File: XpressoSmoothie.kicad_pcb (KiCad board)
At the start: 2 copper layers, 99.7 x 99.7 mm, 130 parts, among them J1 HEADER_4, J10 HEADER_3X2, J11 Pwr_in, J12 HEADER_4, J13 HEADER_4X2, J14 HEADER_3X2, J15 HEADER_4, J16 HEADER_4, J17 HEADER_4, J172 HEADER_2, J18 HEADER_4, J19 HEADER_2, J2 HEADER_4, J20 HEADER_2, J21 HEADER_2, J22 HEADER_2, J23 HEADER_4, J232 HEADER_2, J24 HEADER_4, J25 HEADER_4, J252 HEADER_2, J26 USB, J27 HEADER_4, J28 MICROSD-MOLEX, J3 HEADER_3, J4 HEADER_3X2, J5 HEADER_3X2, J6 LPCXPRESSO_GENERIC_HEADER, J7 HEADER_4, J8 HEADER_4, J9 HEADER_3X2, M1 LOGO_OSHW, M2 LOGO_OSHW, Q1 IRLB 8743, Q2 IRLB 8743, Q3 IRLB 8743, Q4 IRLB 8743, SW1 SW_PUSH, SW2 SW_PUSH, U1 POLOLU_A4988, U10 TC4422A, U11 TC4422A, U12 LM1117-3.3, U2 POLOLU_A4988, U3 POLOLU_A4988, U4 POLOLU_A4988, U5 POLOLU_A4988, U7 LM7809CT, U8 TC4422A, U9 TC4422A

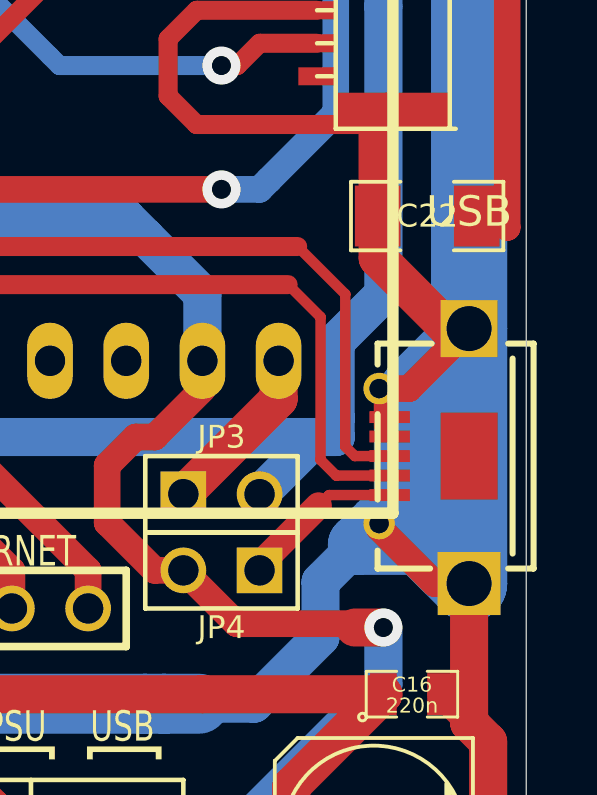
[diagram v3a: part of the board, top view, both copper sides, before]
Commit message: Moved USB so that PCB edge line lines up with the edge of the PCB. Also removed silkscreen lines that hung over the edge. Closes #15.
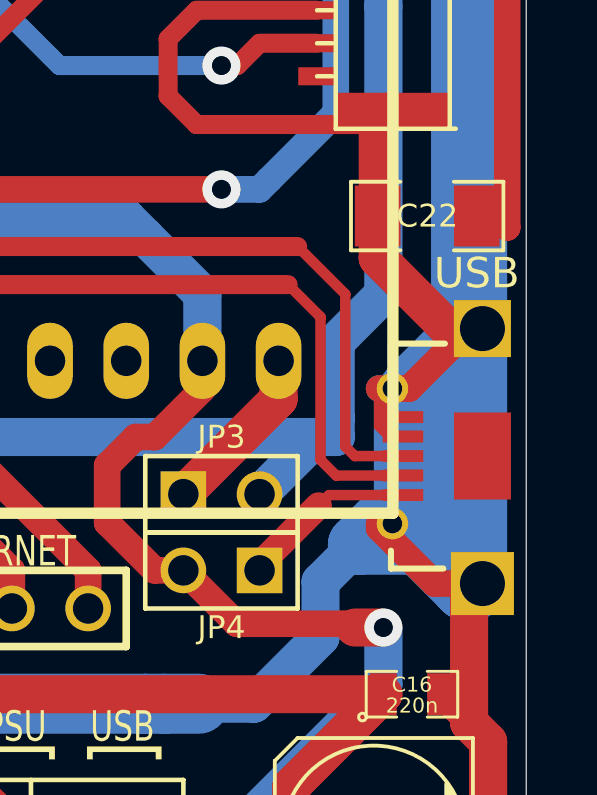
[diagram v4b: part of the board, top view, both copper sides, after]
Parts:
- J26: footprint USB_MICRO_RMC -> USB_MICRO_RMC_noedge
- moved J26 0.44 mm to (170.0, 120.0)
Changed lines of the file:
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@@
     (links 344)
     (no_connects 11)
-    (area 56.388 52.51262 179.864657 163.2712)
+    (area 71.742299 53.962299 171.462701 153.682701)
     (thickness 1.6)
     (drawings 31)
@@
   )
   (setup
-    (last_trace_width 2.54)
+    (last_trace_width 0.635)
     (user_trace_width 0.35)
     (user_trace_width 0.889)
@@
     (add_net ZMIN)
   )
-  (module USB_MICRO_RMC (layer F.Cu)
-    (at 169.545 120.015 180)
-    (fp_text reference J26 (at 0 -7.44982 180) (layer F.SilkS) hide
-      (effects (font (size 1.016 1.016) (thickness 0.127)))
-    )
-    (fp_text value USB (at 0 8.15086 180) (layer F.SilkS)
-      (effects (font (size 1.016 1.016) (thickness 0.127)))
-    )
-    (fp_line (start -1.45034 -3.2512) (end -1.45034 3.2512) (layer F.SilkS) (width 0.2032))
-    (fp_line (start 1.24968 3.74904) (end 3.05054 3.74904) (layer F.SilkS) (width 0.2032))
-    (fp_line (start 3.05054 3.74904) (end 3.05054 3.05054) (layer F.SilkS) (width 0.2032))
-    (fp_line (start 3.05054 -1.45034) (end 3.05054 1.39954) (layer F.SilkS) (width 0.2032))
-    (fp_line (start 1.30048 -3.74904) (end 3.05054 -3.74904) (layer F.SilkS) (width 0.2032))
-    (fp_line (start 3.05054 -3.74904) (end 3.05054 -3.1496) (layer F.SilkS) (width 0.2032))
-    (fp_line (start -2.14884 3.74904) (end -1.30048 3.74904) (layer F.SilkS) (width 0.2032))
-    (fp_line (start -2.14884 3.74904) (end -2.14884 -3.74904) (layer F.SilkS) (width 0.2032))
-    (fp_line (start -2.14884 -3.74904) (end -1.30048 -3.74904) (layer F.SilkS) (width 0.2032))
-    (pad 5 smd rect (at 0 0 180) (size 1.89992 2.90068)
-      (layers F.Cu F.Paste F.Mask)
-      (net 19 GND)
-    )
-    (pad 5 thru_hole rect (at 0 -4.24942 180) (size 2.10058 2.10058) (drill 1.50114)
-      (layers *.Cu *.Mask F.SilkS)
-      (net 19 GND)
-    )
-    (pad 5 thru_hole rect (at 0 4.24942 180) (size 1.89992 1.89992) (drill 1.50114)
-      (layers *.Cu *.Mask F.SilkS)
-      (net 19 GND)
-    )
-    (pad 5 thru_hole circle (at 2.99974 2.25044 180) (size 1.04902 1.04902) (drill 0.65024)
-      (layers *.Cu *.Mask F.SilkS)
-      (net 19 GND)
-    )
-    (pad 5 thru_hole circle (at 2.99974 -2.25044 180) (size 1.04902 1.04902) (drill 0.65024)
-      (layers *.Cu *.Mask F.SilkS)
-      (net 19 GND)
-    )
-    (pad 3 smd rect (at 2.64922 0 180) (size 1.34874 0.39878)
-      (layers F.Cu F.Paste F.Mask)
-      (net 119 USB-D+)
-    )
-    (pad 6 smd rect (at 2.64922 0.65024 180) (size 1.34874 0.39878)
-      (layers F.Cu F.Paste F.Mask)
-      (net 19 GND)
-    )
-    (pad 4 smd rect (at 2.64922 1.30048 180) (size 1.34874 0.39878)
-      (layers F.Cu F.Paste F.Mask)
-      (net 19 GND)
-    )
-    (pad 2 smd rect (at 2.64922 -0.65024 180) (size 1.34874 0.39878)
-      (layers F.Cu F.Paste F.Mask)
-      (net 120 USB-D-)
-    )
-    (pad 1 smd rect (at 2.64922 -1.30048 180) (size 1.34874 0.39878)
-      (layers F.Cu F.Paste F.Mask)
-      (net 52 N-0000014)
-    )
-    (model ..\KiCAD_Libraries\packages3d\rmc\misc\USB3075-30-Ak.wrl
-      (at (xyz 0.165 -0.155 0))
-      (scale (xyz 1 1 1))
-      (rotate (xyz 0 180 0))
-    )
-  )
   (module TO220_VERT_C (layer F.Cu)
     (at 92.202 137.795 270)
@@
     )
   )
+  (module USB_MICRO_RMC_noedge (layer F.Cu)
+    (at 169.9895 120.015 180)
+    (fp_text reference J26 (at 0 -7.44982 180) (layer F.SilkS) hide
+      (effects (font (size 1.016 1.016) (thickness 0.127)))
+    )
+    (fp_text value USB (at 0.1905 6.096 180) (layer F.SilkS)
+      (effects (font (size 1.016 1.016) (thickness 0.127)))
+    )
+    (fp_line (start 1.24968 3.74904) (end 3.05054 3.74904) (layer F.SilkS) (width 0.2032))
+    (fp_line (start 3.05054 3.74904) (end 3.05054 3.05054) (layer F.SilkS) (width 0.2032))
+    (fp_line (start 3.05054 -1.45034) (end 3.05054 1.39954) (layer F.SilkS) (width 0.2032))
+    (fp_line (start 1.30048 -3.74904) (end 3.05054 -3.74904) (layer F.SilkS) (width 0.2032))
+    (fp_line (start 3.05054 -3.74904) (end 3.05054 -3.1496) (layer F.SilkS) (width 0.2032))
+    (pad 5 smd rect (at 0 0 180) (size 1.89992 2.90068)
+      (layers F.Cu F.Paste F.Mask)
+      (net 19 GND)
+    )
+    (pad 5 thru_hole rect (at 0 -4.24942 180) (size 2.10058 2.10058) (drill 1.50114)
+      (layers *.Cu *.Mask F.SilkS)
+      (net 19 GND)
+    )
+    (pad 5 thru_hole rect (at 0 4.24942 180) (size 1.89992 1.89992) (drill 1.50114)
+      (layers *.Cu *.Mask F.SilkS)
+      (net 19 GND)
+    )
+    (pad 5 thru_hole circle (at 2.99974 2.25044 180) (size 1.04902 1.04902) (drill 0.65024)
+      (layers *.Cu *.Mask F.SilkS)
+      (net 19 GND)
+    )
+    (pad 5 thru_hole circle (at 2.99974 -2.25044 180) (size 1.04902 1.04902) (drill 0.65024)
+      (layers *.Cu *.Mask F.SilkS)
+      (net 19 GND)
+    )
+    (pad 3 smd rect (at 2.64922 0 180) (size 1.34874 0.39878)
+      (layers F.Cu F.Paste F.Mask)
+      (net 119 USB-D+)
+    )
+    (pad 6 smd rect (at 2.64922 0.65024 180) (size 1.34874 0.39878)
+      (layers F.Cu F.Paste F.Mask)
+      (net 19 GND)
+    )
+    (pad 4 smd rect (at 2.64922 1.30048 180) (size 1.34874 0.39878)
+      (layers F.Cu F.Paste F.Mask)
+      (net 19 GND)
+    )
+    (pad 2 smd rect (at 2.64922 -0.65024 180) (size 1.34874 0.39878)
+      (layers F.Cu F.Paste F.Mask)
+      (net 120 USB-D-)
+    )
+    (pad 1 smd rect (at 2.64922 -1.30048 180) (size 1.34874 0.39878)
+      (layers F.Cu F.Paste F.Mask)
+      (net 52 N-0000014)
+    )
+    (model ..\KiCAD_Libraries\packages3d\rmc\misc\USB3075-30-Ak.wrl
+      (at (xyz 0.165 -0.155 0))
+      (scale (xyz 1 1 1))
+      (rotate (xyz 0 180 0))
+    )
+  )
   (gr_text MISC (at 144.145 152.4) (layer F.SilkS)
     (effects (font (size 2.032 1.524) (thickness 0.3048)))
@@
   (segment (start 157.7975 134.3025) (end 160.02 134.3025) (width 1.27) (layer F.Cu) (net 79))
   (segment (start 156.21 132.715) (end 157.7975 134.3025) (width 1.27) (layer F.Cu) (net 79))
-  (segment (start 84.074 136.271) (end 84.074 139.7) (width 2.54) (layer B.Cu) (net 80) (status 400000))
+  (segment (start 84.074 136.271) (end 84.074 139.7) (width 2.54) (layer B.Cu) (net 80))
   (segment (start 84.074 139.7) (end 84.074 137.16) (width 3.81) (layer B.Cu) (net 80))
   (segment (start 84.074 137.16) (end 84.074 136.525) (width 2.54) (layer B.Cu) (net 80))

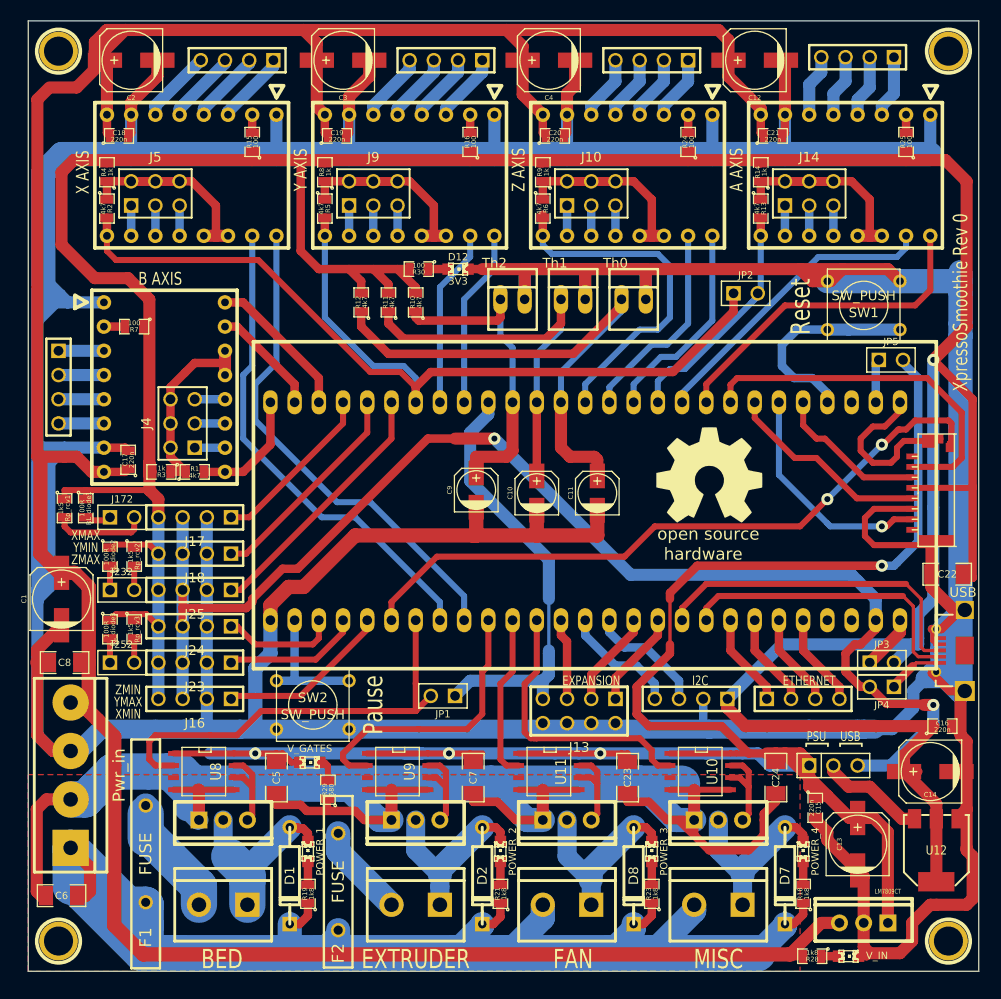
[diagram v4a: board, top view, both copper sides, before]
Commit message: Moved some traces and text so that there is a minimum of 10 mil clearnace between any traces or pads and the pcb edge. Closes #16.
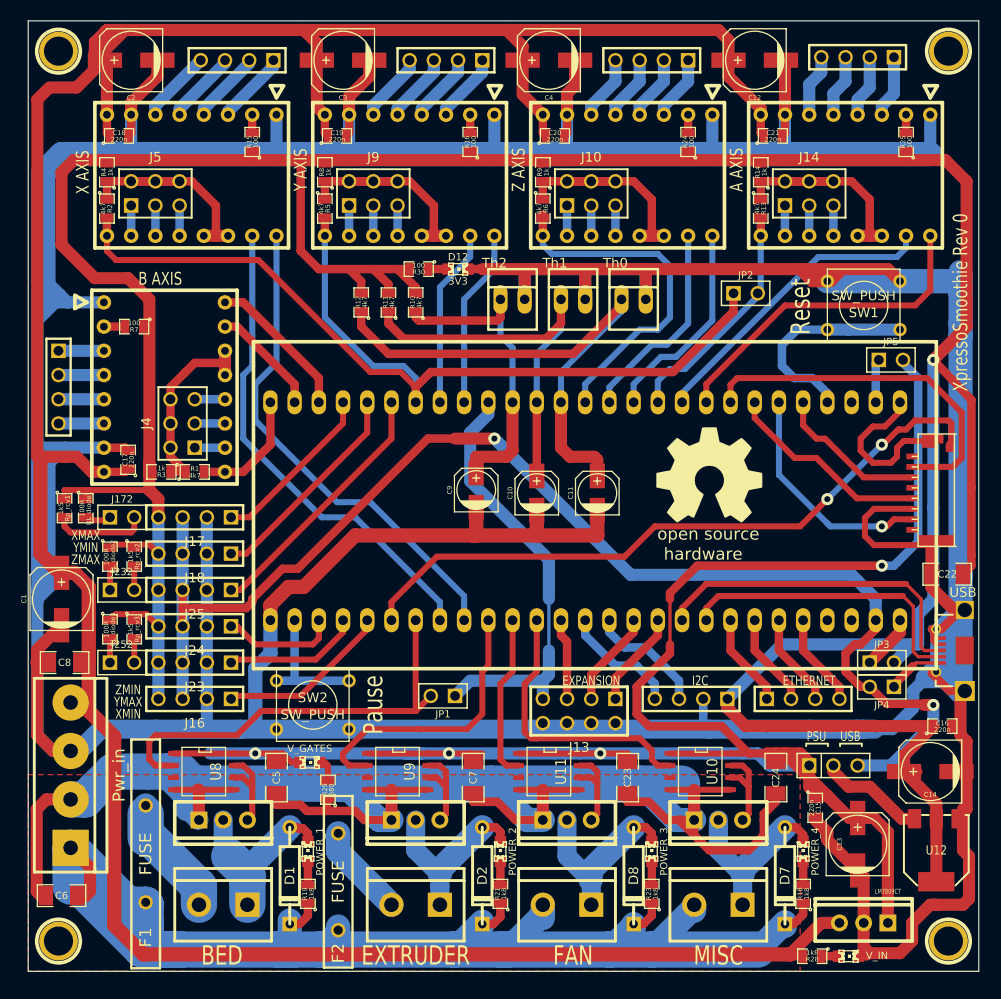
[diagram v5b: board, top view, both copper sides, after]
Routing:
- net +3.3VP: track 377.7 -> 370.1 mm

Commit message: Spruced up the labels a bit.
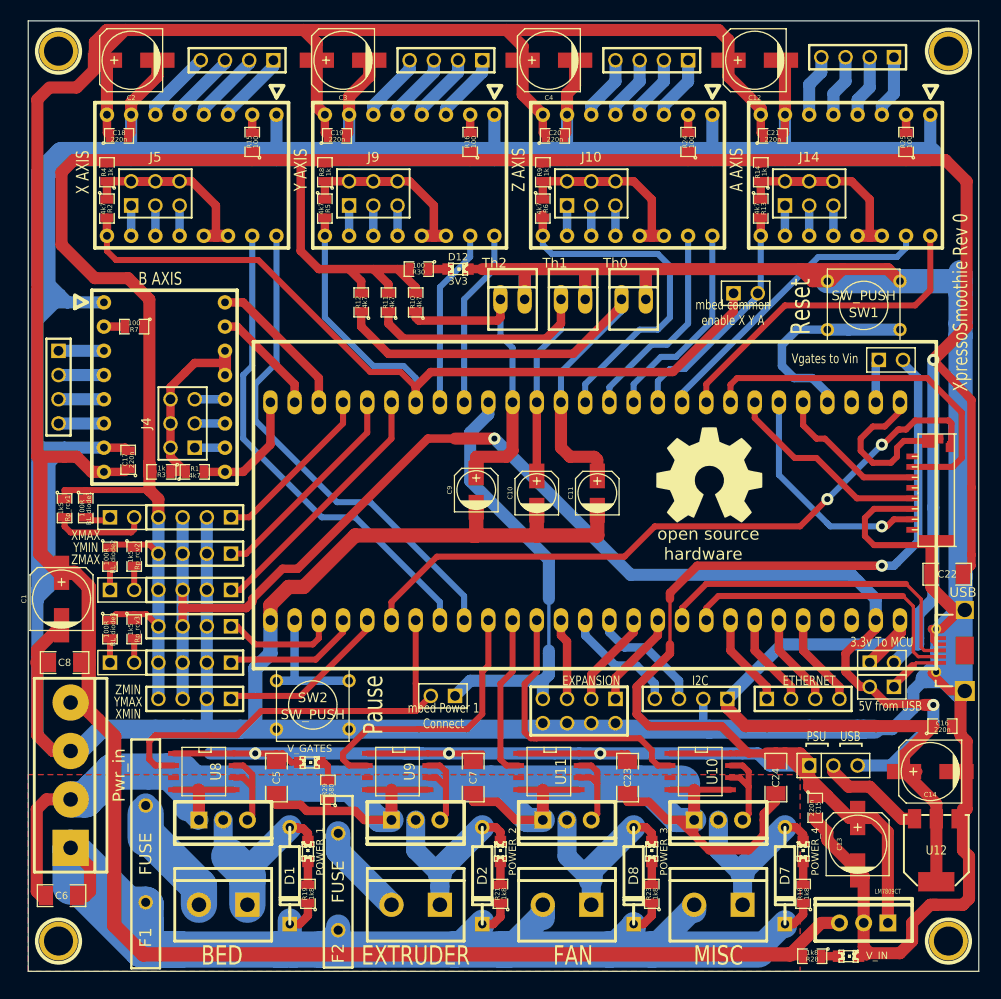
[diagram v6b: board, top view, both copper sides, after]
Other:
- board text added: "3.3v To MCU"
- board text added: "5V from USB"
- board text added: "Vgates to Vin"
- board text added: "mbed Power 1 Connect"
- board text added: "mbed common enable X Y A"
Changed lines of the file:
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@@
     (area 56.388 52.51262 179.864657 163.2712)
     (thickness 1.6)
-    (drawings 31)
+    (drawings 36)
     (tracks 1193)
     (zones 0)
@@
   )
   (layers
-    (15 F.Cu signal hide)
-    (0 B.Cu signal)
+    (15 F.Cu signal)
+    (0 B.Cu signal hide)
     (16 B.Adhes user)
     (17 F.Adhes user)
@@
   )
   (setup
-    (last_trace_width 0.889)
+    (last_trace_width 0.635)
     (user_trace_width 0.35)
     (user_trace_width 0.889)
@@
     (pad_to_mask_clearance 0.254)
     (aux_axis_origin 0 0)
-    (visible_elements 7FFFFB3F)
+    (visible_elements 7FFFFA3F)
     (pcbplotparams
       (layerselection 15761409)
@@
     (descr "Connecteurs 2 pins")
     (tags "CONN DEV")
-    (fp_text reference JP1 (at 0 -1.905 180) (layer F.SilkS)
+    (fp_text reference JP1 (at 0 -1.905 180) (layer F.SilkS) hide
       (effects (font (size 0.762 0.762) (thickness 0.1524)))
     )
@@
     (descr "Connecteurs 2 pins")
     (tags "CONN DEV")
-    (fp_text reference JP2 (at 0 -1.905) (layer F.SilkS)
+    (fp_text reference JP2 (at 0 -1.905) (layer F.SilkS) hide
       (effects (font (size 0.762 0.762) (thickness 0.1524)))
     )
@@
     (descr "Double rangee de contacts 2 x 4 pins")
     (tags CONN)
-    (fp_text reference J13 (at 0 -3.81 180) (layer F.SilkS)
+    (fp_text reference J13 (at 0 -3.81 180) (layer F.SilkS) hide
       (effects (font (size 1.016 1.016) (thickness 0.2032)))
     )
@@
     (descr "Connecteurs 2 pins")
     (tags "CONN DEV")
-    (fp_text reference JP3 (at 0 -1.905) (layer F.SilkS)
+    (fp_text reference JP3 (at 0 -1.905) (layer F.SilkS) hide
       (effects (font (size 0.762 0.762) (thickness 0.1524)))
     )
@@
     (descr "Connecteurs 2 pins")
     (tags "CONN DEV")
-    (fp_text reference JP5 (at 0 -1.905) (layer F.SilkS)
+    (fp_text reference JP5 (at 0 -1.905) (layer F.SilkS) hide
       (effects (font (size 0.762 0.762) (thickness 0.1524)))
     )
@@
     (descr "Double rangee de contacts 2 x 5 pins")
     (tags CONN)
-    (fp_text reference J16 (at 0 -2.54 180) (layer F.SilkS)
+    (fp_text reference J16 (at 0 -2.54 180) (layer F.SilkS) hide
       (effects (font (size 1.016 1.016) (thickness 0.2032)))
     )
@@
     (descr "Double rangee de contacts 2 x 5 pins")
     (tags CONN)
-    (fp_text reference J18 (at 0 -2.54 180) (layer F.SilkS)
+    (fp_text reference J18 (at 0 -2.54 180) (layer F.SilkS) hide
       (effects (font (size 1.016 1.016) (thickness 0.2032)))
     )
@@
     (descr "Double rangee de contacts 2 x 5 pins")
     (tags CONN)
-    (fp_text reference J24 (at 0 -2.54 180) (layer F.SilkS)
+    (fp_text reference J24 (at 0 -2.54 180) (layer F.SilkS) hide
       (effects (font (size 1.016 1.016) (thickness 0.2032)))
     )
@@
     (descr "Connecteurs 2 pins")
     (tags "CONN DEV")
-    (fp_text reference J172 (at 0 -1.905) (layer F.SilkS)
+    (fp_text reference J172 (at 0 -1.905) (layer F.SilkS) hide
       (effects (font (size 0.762 0.762) (thickness 0.1524)))
     )
@@
     (descr "Connecteurs 2 pins")
     (tags "CONN DEV")
-    (fp_text reference J232 (at 0 -1.905) (layer F.SilkS)
+    (fp_text reference J232 (at 0 -1.905) (layer F.SilkS) hide
       (effects (font (size 0.762 0.762) (thickness 0.1524)))
     )
@@
     (descr "Connecteurs 2 pins")
     (tags "CONN DEV")
-    (fp_text reference J252 (at 0 -1.905) (layer F.SilkS)
+    (fp_text reference J252 (at 0 -1.905) (layer F.SilkS) hide
       (effects (font (size 0.762 0.762) (thickness 0.1524)))
     )
@@
     (descr "Double rangee de contacts 2 x 5 pins")
     (tags CONN)
-    (fp_text reference J17 (at 0 -2.54 180) (layer F.SilkS)
+    (fp_text reference J17 (at 0 -2.54 180) (layer F.SilkS) hide
       (effects (font (size 1.016 1.016) (thickness 0.2032)))
     )
@@
     (descr "Double rangee de contacts 2 x 5 pins")
     (tags CONN)
-    (fp_text reference J23 (at 0 -2.54 180) (layer F.SilkS)
+    (fp_text reference J23 (at 0 -2.54 180) (layer F.SilkS) hide
       (effects (font (size 1.016 1.016) (thickness 0.2032)))
     )
@@
     (descr "Double rangee de contacts 2 x 5 pins")
     (tags CONN)
-    (fp_text reference J25 (at 0 -2.54 180) (layer F.SilkS)
+    (fp_text reference J25 (at 0 -2.54 180) (layer F.SilkS) hide
       (effects (font (size 1.016 1.016) (thickness 0.2032)))
     )
@@
     (descr "Connecteurs 2 pins")
     (tags "CONN DEV")
-    (fp_text reference JP4 (at 0 -1.905 180) (layer F.SilkS)
+    (fp_text reference JP4 (at 0 -1.905 180) (layer F.SilkS) hide
       (effects (font (size 0.762 0.762) (thickness 0.1524)))
     )
@@
     )
   )
+  (gr_text "Vgates to Vin" (at 155.321 89.408) (layer F.SilkS)
+    (effects (font (size 1.016 0.762) (thickness 0.1524)))
+  )
+  (gr_text "mbed common\nenable X Y A" (at 145.669 84.582) (layer F.SilkS)
+    (effects (font (size 1.016 0.762) (thickness 0.1524)))
+  )
+  (gr_text "mbed Power 1\nConnect" (at 115.316 126.873) (layer F.SilkS)
+    (effects (font (size 1.016 0.762) (thickness 0.1524)))
+  )
+  (gr_text "5V from USB" (at 162.179 125.857) (layer F.SilkS)
+    (effects (font (size 1.016 0.762) (thickness 0.1524)))
+  )
+  (gr_text "3.3v To MCU" (at 161.29 119.126) (layer F.SilkS)
+    (effects (font (size 1.016 0.762) (thickness 0.1524)))
+  )
   (gr_text MISC (at 144.145 152.019) (layer F.SilkS)

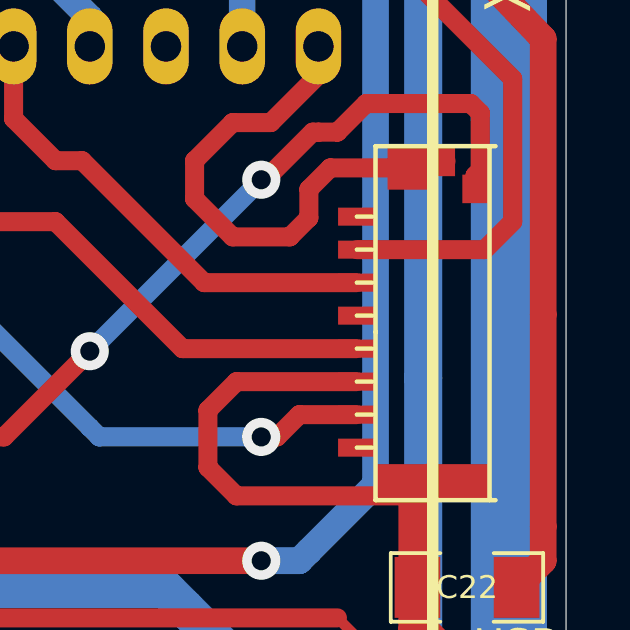
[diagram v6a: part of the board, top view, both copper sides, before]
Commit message: D'oh, cut the 3.3v line to card reader. Fixed.
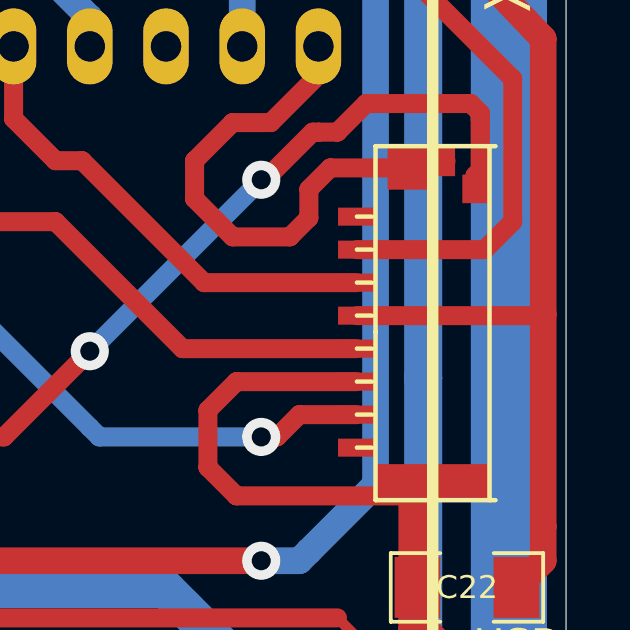
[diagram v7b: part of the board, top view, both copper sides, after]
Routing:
- net +3.3VP: track 370.1 -> 376.3 mm
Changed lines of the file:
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@@
   (general
     (links 344)
-    (no_connects 12)
+    (no_connects 11)
     (area 56.388 52.51262 179.864657 163.2712)
     (thickness 1.6)
     (drawings 36)
-    (tracks 1193)
+    (tracks 1195)
     (zones 0)
     (modules 130)
@@
     (arrow2b (pts (xy 64.770001 53.975) (xy 65.356421 55.101503)))
   )
+  (segment (start 164.475 102.955) (end 170.688 102.955) (width 0.635) (layer F.Cu) (net 1) (status 400000))
+  (segment (start 170.688 102.955) (end 170.688 102.912) (width 0.635) (layer F.Cu) (net 1))
   (segment (start 170.688 109.982) (end 170.688 111.125) (width 0.889) (layer F.Cu) (net 1))
   (segment (start 170.688 102.912) (end 170.688 109.982) (width 0.889) (layer F.Cu) (net 1))
